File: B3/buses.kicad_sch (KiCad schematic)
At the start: 3 parts

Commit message: B1 CREGA added
Work started on b1. CREGA added.
Minor changes to B0 schematic properties.
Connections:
- net ~EN10 renamed ~{EN10}
- net ~EN11 renamed ~{EN11}
- net ~EN12 renamed ~{EN12}
- net ~EN13 renamed ~{EN13}
- net ~EN14 renamed ~{EN14}
- net ~EN15 renamed ~{EN15}
- net ~EN4 renamed ~{EN4}
- net ~EN5 renamed ~{EN5}
- net ~EN6 renamed ~{EN6}
- net ~EN7 renamed ~{EN7}
- net ~EN8 renamed ~{EN8}
- net ~EN9 renamed ~{EN9}
- net ~FLAG renamed ~{FLAG}
- net ~IRQ renamed ~{IRQ}
- net ~RES renamed ~{RES}

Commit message: Updates to B3
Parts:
- ENABLEBUS3: renamed from ENABLEBUS2; value Conn_02x10_Odd_Even -> (none); footprint Connector_PinHeader_2.54mm:PinHeader_2x10_P2.54mm_Vertical -> (none)
- renumbered CONTROLBUS2 to CONTROLBUS3, DATABUS2 to DATABUS3
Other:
- title: (none) -> 74HCT6526 Board 3
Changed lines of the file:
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@@
 (kicad_sch (version 20211123) (generator eeschema)
   (paper "A4")
+  (title_block
+    (title "74HCT6526 Board 3")
+    (date "2022-09-11")
+    (rev "0.1")
+  )
   (junction (at 111.76 83.82) (diameter 1.016) (color 0 0 0 0)
   )
@@
   (junction (at 134.62 35.56) (diameter 1.016) (color 0 0 0 0)
   )
+  (junction (at 134.62 96.52) (diameter 0) (color 0 0 0 0)
+  )
   (bus_entry (at 78.74 83.82) (size 2.54 2.54)
     (stroke (width 0.1524) (type solid) (color 0 0 0 0))
@@
     (stroke (width 0) (type solid) (color 0 0 0 0))
   )
+  (bus (pts (xy 180.34 88.9) (xy 180.34 96.52))
+    (stroke (width 0) (type default) (color 0 0 0 0))
+  )
   (wire (pts (xy 210.82 91.44) (xy 226.06 91.44))
     (stroke (width 0) (type solid) (color 0 0 0 0))
@@
     (stroke (width 0) (type solid) (color 0 0 0 0))
   )
-  (bus (pts (xy 180.34 73.66) (xy 180.34 81.28))
-    (stroke (width 0) (type solid) (color 0 0 0 0))
-  )
   (wire (pts (xy 165.1 76.2) (xy 177.8 76.2))
     (stroke (width 0) (type solid) (color 0 0 0 0))
@@
     (stroke (width 0) (type solid) (color 0 0 0 0))
   )
-  (bus (pts (xy 134.62 73.66) (xy 134.62 81.28))
-    (stroke (width 0) (type solid) (color 0 0 0 0))
-  )
   (wire (pts (xy 238.76 68.58) (xy 256.54 68.58))
     (stroke (width 0) (type solid) (color 0 0 0 0))
@@
     (stroke (width 0) (type solid) (color 0 0 0 0))
   )
+  (bus (pts (xy 134.62 96.52) (xy 134.62 88.9))
+    (stroke (width 0) (type default) (color 0 0 0 0))
+  )
   (bus (pts (xy 180.34 35.56) (xy 180.34 66.04))
     (stroke (width 0) (type solid) (color 0 0 0 0))
@@
     (stroke (width 0) (type solid) (color 0 0 0 0))
   )
+  (bus (pts (xy 27.94 96.52) (xy 134.62 96.52))
+    (stroke (width 0) (type default) (color 0 0 0 0))
+  )
   (wire (pts (xy 165.1 71.12) (xy 177.8 71.12))
     (stroke (width 0) (type solid) (color 0 0 0 0))
@@
     (stroke (width 0) (type solid) (color 0 0 0 0))
   )
+  (bus (pts (xy 180.34 96.52) (xy 134.62 96.52))
+    (stroke (width 0) (type default) (color 0 0 0 0))
+  )
   (wire (pts (xy 81.28 71.12) (xy 99.06 71.12))
     (stroke (width 0) (type solid) (color 0 0 0 0))
@@
     (effects (font (size 1.27 1.27)) (justify right bottom))
   )
-  (label "{ENABLEBUS}" (at 132.08 38.1 180)
-    (effects (font (size 1.27 1.27)) (justify right bottom))
-  )
   (label "D5" (at 147.32 71.12 180)
     (effects (font (size 1.27 1.27)) (justify right bottom))
@@
     (effects (font (size 1.27 1.27)) (justify right bottom))
   )
-  (label "{DATABUS}" (at 180.34 35.56 180)
-    (effects (font (size 1.27 1.27)) (justify right bottom))
-  )
   (label "~{EN9}" (at 91.44 86.36 180)
     (effects (font (size 1.27 1.27)) (justify right bottom))
@@
     (effects (font (size 1.27 1.27)) (justify right bottom))
   )
-  (hierarchical_label "{DATABUS}" (shape bidirectional) (at 27.94 35.56 180)
+  (hierarchical_label "D[0..7]" (shape input) (at 27.94 35.56 180)
+    (effects (font (size 1.27 1.27)) (justify right))
+  )
+  (hierarchical_label "DZ[0..7]" (shape output) (at 27.94 96.52 180)
     (effects (font (size 1.27 1.27)) (justify right))
   )
@@
     (effects (font (size 1.27 1.27)) (justify right))
   )
-  (hierarchical_label "{ENABLEBUS}" (shape input) (at 27.94 38.1 180)
+  (hierarchical_label "~{EN[0..15]}" (shape output) (at 27.94 38.1 180)
     (effects (font (size 1.27 1.27)) (justify right))
   )
@@
       (effects (font (size 1.27 1.27)) hide)
     )
-    (property "Value" "VCC" (id 1) (at 118.4783 76.9556 0))
+    (property "Value" "" (id 1) (at 118.4783 76.9556 0))
     (property "Footprint" "" (id 2) (at 118.11 81.28 0)
       (effects (font (size 1.27 1.27)) hide)
@@
   (symbol (lib_id "Connector_Generic:Conn_02x10_Odd_Even") (at 104.14 78.74 0) (unit 1)
     (in_bom yes) (on_board yes)
-    (property "Reference" "ENABLEBUS2" (id 0) (at 105.41 63.1 0))
-    (property "Value" "Conn_02x10_Odd_Even" (id 1) (at 105.41 65.3985 0))
-    (property "Footprint" "Connector_PinHeader_2.54mm:PinHeader_2x10_P2.54mm_Vertical" (id 2) (at 104.14 78.74 0)
+    (property "Reference" "ENABLEBUS3" (id 0) (at 105.41 63.1 0))
+    (property "Value" "" (id 1) (at 105.41 65.3985 0))
+    (property "Footprint" "" (id 2) (at 104.14 78.74 0)
       (effects (font (size 1.27 1.27)) hide)
     )
@@
       (effects (font (size 1.27 1.27)) hide)
     )
-    (property "Value" "VCC" (id 1) (at 142.6083 76.9556 0))
+    (property "Value" "" (id 1) (at 142.6083 76.9556 0))
     (property "Footprint" "" (id 2) (at 142.24 81.28 0)
       (effects (font (size 1.27 1.27)) hide)
@@
   (symbol (lib_id "Connector_Generic:Conn_02x10_Odd_Even") (at 231.14 78.74 0) (unit 1)
     (in_bom yes) (on_board yes)
-    (property "Reference" "CONTROLBUS2" (id 0) (at 232.41 63.1 0))
+    (property "Reference" "CONTROLBUS3" (id 0) (at 232.41 63.1 0))
     (property "Value" "Conn_02x10_Odd_Even" (id 1) (at 232.41 65.3985 0))
     (property "Footprint" "Connector_PinHeader_2.54mm:PinHeader_2x10_P2.54mm_Vertical" (id 2) (at 231.14 78.74 0)
@@
   (symbol (lib_id "Connector_Generic:Conn_02x10_Odd_Even") (at 157.48 78.74 0) (unit 1)
     (in_bom yes) (on_board yes)
-    (property "Reference" "DATABUS2" (id 0) (at 158.75 63.1 0))
+    (property "Reference" "DATABUS3" (id 0) (at 158.75 63.1 0))
     (property "Value" "Conn_02x10_Odd_Even" (id 1) (at 158.75 65.3985 0))
     (property "Footprint" "Connector_PinHeader_2.54mm:PinHeader_2x10_P2.54mm_Vertical" (id 2) (at 157.48 78.74 0)
@@
       (effects (font (size 1.27 1.27)) hide)
     )
-    (property "Value" "GND" (id 1) (at 118.2243 88.1444 0))
+    (property "Value" "" (id 1) (at 118.2243 88.1444 0))
     (property "Footprint" "" (id 2) (at 118.11 83.82 0)
       (effects (font (size 1.27 1.27)) hide)
@@
       (effects (font (size 1.27 1.27)) hide)
     )
-    (property "Value" "GND" (id 1) (at 175.3743 83.0644 0))
+    (property "Value" "" (id 1) (at 175.3743 83.0644 0))
     (property "Footprint" "" (id 2) (at 175.26 78.74 0)
       (effects (font (size 1.27 1.27)) hide)

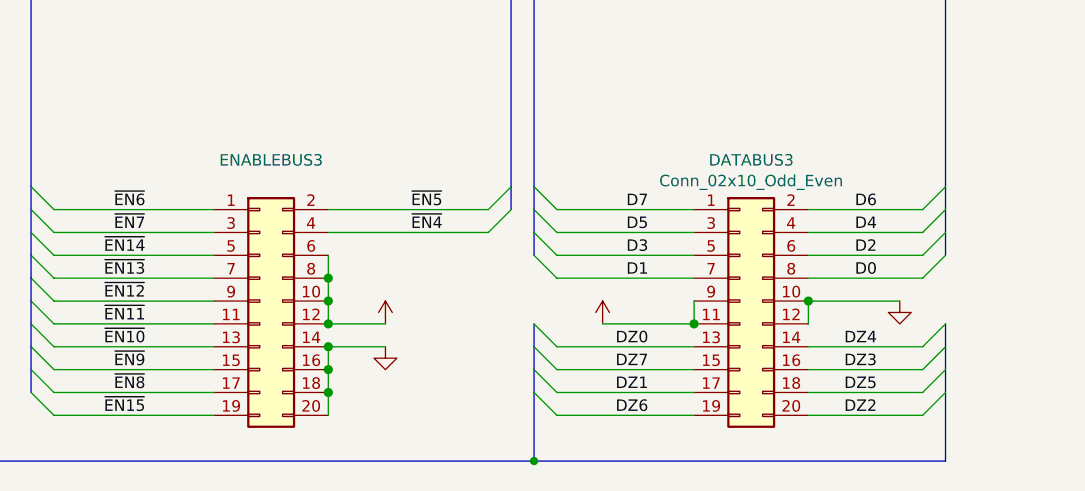
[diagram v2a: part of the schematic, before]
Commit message: B3 added. First revision
Still not verified.
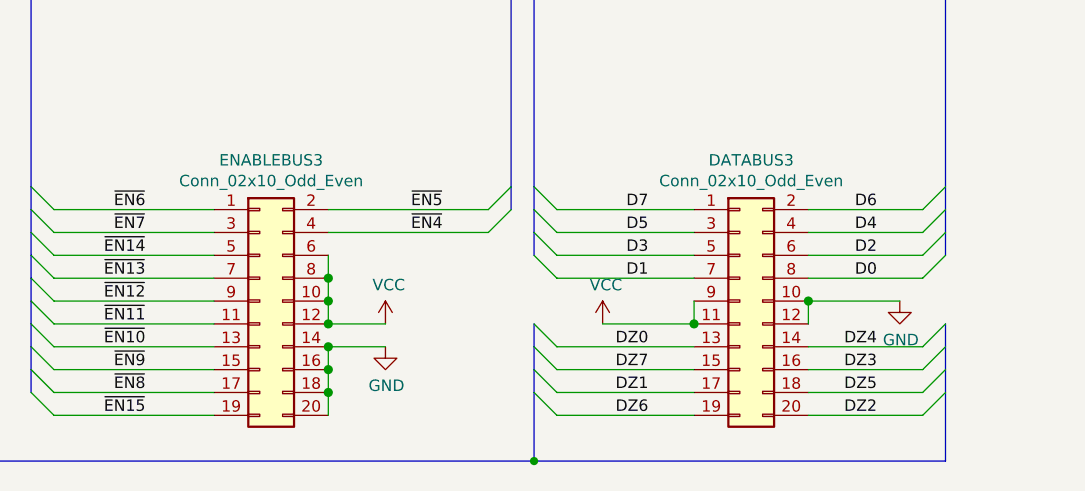
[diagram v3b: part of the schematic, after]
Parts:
- ENABLEBUS3: value (none) -> Conn_02x10_Odd_Even; footprint (none) -> Connector_PinHeader_2.54mm:PinHeader_2x10_P2.54mm_Vertical
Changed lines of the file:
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@@
       (effects (font (size 1.27 1.27)) hide)
     )
-    (property "Value" "" (id 1) (at 118.4783 76.9556 0))
+    (property "Value" "VCC" (id 1) (at 118.4783 76.9556 0))
     (property "Footprint" "" (id 2) (at 118.11 81.28 0)
       (effects (font (size 1.27 1.27)) hide)
@@
     (in_bom yes) (on_board yes)
     (property "Reference" "ENABLEBUS3" (id 0) (at 105.41 63.1 0))
-    (property "Value" "" (id 1) (at 105.41 65.3985 0))
-    (property "Footprint" "" (id 2) (at 104.14 78.74 0)
+    (property "Value" "Conn_02x10_Odd_Even" (id 1) (at 105.41 65.3985 0))
+    (property "Footprint" "Connector_PinHeader_2.54mm:PinHeader_2x10_P2.54mm_Vertical" (id 2) (at 104.14 78.74 0)
       (effects (font (size 1.27 1.27)) hide)
     )
@@
       (effects (font (size 1.27 1.27)) hide)
     )
-    (property "Value" "" (id 1) (at 142.6083 76.9556 0))
+    (property "Value" "VCC" (id 1) (at 142.6083 76.9556 0))
     (property "Footprint" "" (id 2) (at 142.24 81.28 0)
       (effects (font (size 1.27 1.27)) hide)
@@
       (effects (font (size 1.27 1.27)) hide)
     )
-    (property "Value" "" (id 1) (at 118.2243 88.1444 0))
+    (property "Value" "GND" (id 1) (at 118.2243 88.1444 0))
     (property "Footprint" "" (id 2) (at 118.11 83.82 0)
       (effects (font (size 1.27 1.27)) hide)
@@
       (effects (font (size 1.27 1.27)) hide)
     )
-    (property "Value" "" (id 1) (at 175.3743 83.0644 0))
+    (property "Value" "GND" (id 1) (at 175.3743 83.0644 0))
     (property "Footprint" "" (id 2) (at 175.26 78.74 0)
       (effects (font (size 1.27 1.27)) hide)

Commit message: .
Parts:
- added C340: 100n, Capacitor_SMD:C_0603_1608Metric, symbol Device:C
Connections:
- net GND: now also C340.2
- net ~{RES}: now also C340.1
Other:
- company: (none) -> Daniel Molina
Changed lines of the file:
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@@
   (title_block
     (title "74HCT6526 Board 3")
-    (date "2022-09-11")
-    (rev "0.1")
+    (date "2022-10-08")
+    (rev "0.1.2")
+    (company "Daniel Molina")
+    (comment 1 "https://github.com/dmolinagarcia/74HCT6526")
   )
   (junction (at 111.76 83.82) (diameter 1.016) (color 0 0 0 0)
@@
   (junction (at 111.76 81.28) (diameter 1.016) (color 0 0 0 0)
   )
+  (junction (at 245.11 91.44) (diameter 0) (color 0 0 0 0)
+  )
   (junction (at 78.74 38.1) (diameter 1.016) (color 0 0 0 0)
   )
@@
     (stroke (width 0) (type solid) (color 0 0 0 0))
   )
-  (wire (pts (xy 238.76 91.44) (xy 256.54 91.44))
+  (wire (pts (xy 238.76 91.44) (xy 245.11 91.44))
     (stroke (width 0) (type solid) (color 0 0 0 0))
   )
@@
   )
   (bus (pts (xy 259.08 83.82) (xy 259.08 86.36))
+    (stroke (width 0) (type solid) (color 0 0 0 0))
+  )
+  (wire (pts (xy 245.11 91.44) (xy 256.54 91.44))
     (stroke (width 0) (type solid) (color 0 0 0 0))
   )
@@
     (pin "9")
   )
+  (symbol (lib_id "Device:C") (at 245.11 95.25 0) (unit 1)
+    (in_bom yes) (on_board yes) (fields_autoplaced)
+    (property "Reference" "C340" (id 0) (at 248.92 93.9799 0)
+      (effects (font (size 1.27 1.27)) (justify left))
+    )
+    (property "Value" "100n" (id 1) (at 248.92 96.5199 0)
+      (effects (font (size 1.27 1.27)) (justify left))
+    )
+    (property "Footprint" "Capacitor_SMD:C_0603_1608Metric" (id 2) (at 246.0752 99.06 0)
+      (effects (font (size 1.27 1.27)) hide)
+    )
+    (property "Datasheet" "~" (id 3) (at 245.11 95.25 0)
+      (effects (font (size 1.27 1.27)) hide)
+    )
+    (pin "1")
+    (pin "2")
+  )
   (symbol (lib_id "power:GND") (at 118.11 83.82 0) (unit 1)
     (in_bom yes) (on_board yes)
@@
       (effects (font (size 1.27 1.27)) hide)
     )
+    (pin "1")
+  )
+  (symbol (lib_id "power:GND") (at 245.11 99.06 0) (unit 1)
+    (in_bom yes) (on_board yes) (fields_autoplaced)
+    (property "Reference" "#PWR0107" (id 0) (at 245.11 105.41 0)
+      (effects (font (size 1.27 1.27)) hide)
+    )
+    (property "Value" "GND" (id 1) (at 245.11 104.14 0))
+    (property "Footprint" "" (id 2) (at 245.11 99.06 0)
+      (effects (font (size 1.27 1.27)) hide)
+    )
+    (property "Datasheet" "" (id 3) (at 245.11 99.06 0)
+      (effects (font (size 1.27 1.27)) hide)
+    )

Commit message: B0 ready for v0.2.0 release.
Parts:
- renumbered C340 to C300
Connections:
- net TARUNMODE: no longer names the net of CONTROLBUS3.18 (Pin_18)
- no-connect marks 0 -> 1
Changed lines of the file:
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@@
   (title_block
     (title "74HCT6526 Board 3")
-    (date "2022-10-08")
-    (rev "0.1.2")
+    (date "2023-01-22")
+    (rev "0.2.0")
     (company "Daniel Molina")
     (comment 1 "https://github.com/dmolinagarcia/74HCT6526")
@@
   (junction (at 134.62 96.52) (diameter 0) (color 0 0 0 0)
   )
+  (no_connect (at 238.76 88.9))
   (bus_entry (at 78.74 83.82) (size 2.54 2.54)
     (stroke (width 0.1524) (type solid) (color 0 0 0 0))
@@
     (stroke (width 0.1524) (type solid) (color 0 0 0 0))
   )
-  (bus_entry (at 259.08 86.36) (size -2.54 2.54)
-    (stroke (width 0.1524) (type solid) (color 0 0 0 0))
-  )
   (bus_entry (at 134.62 68.58) (size 2.54 2.54)
     (stroke (width 0.1524) (type solid) (color 0 0 0 0))
@@
   )
   (wire (pts (xy 238.76 91.44) (xy 245.11 91.44))
-    (stroke (width 0) (type solid) (color 0 0 0 0))
-  )
-  (wire (pts (xy 238.76 88.9) (xy 256.54 88.9))
     (stroke (width 0) (type solid) (color 0 0 0 0))
   )
@@
     (stroke (width 0) (type solid) (color 0 0 0 0))
   )
-  (bus (pts (xy 259.08 83.82) (xy 259.08 86.36))
+  (bus (pts (xy 259.08 83.82) (xy 259.08 88.9))
     (stroke (width 0) (type solid) (color 0 0 0 0))
   )
@@
     (stroke (width 0) (type solid) (color 0 0 0 0))
   )
-  (bus (pts (xy 259.08 86.36) (xy 259.08 88.9))
-    (stroke (width 0) (type solid) (color 0 0 0 0))
-  )
   (wire (pts (xy 111.76 81.28) (xy 118.11 81.28))
     (stroke (width 0) (type solid) (color 0 0 0 0))
@@
   )
   (label "DZ6" (at 147.32 91.44 180)
-    (effects (font (size 1.27 1.27)) (justify right bottom))
-  )
-  (label "TARUNMODE" (at 251.46 88.9 180)
     (effects (font (size 1.27 1.27)) (justify right bottom))
   )
@@
   (symbol (lib_id "Device:C") (at 245.11 95.25 0) (unit 1)
     (in_bom yes) (on_board yes) (fields_autoplaced)
-    (property "Reference" "C340" (id 0) (at 248.92 93.9799 0)
+    (property "Reference" "C300" (id 0) (at 248.92 93.9799 0)
       (effects (font (size 1.27 1.27)) (justify left))
     )
